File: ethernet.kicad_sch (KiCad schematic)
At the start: 44 parts, among them J6 Bus_RJ45_5-2337992-8, Q17 PJE138K, U22 TPS2372-3RGWR, U23 ULS-12_5-D48N-C, U39 ACPL-217-500E

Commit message: Init commit
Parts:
- C52, C78: LCSC Part # (none) -> C85960
- C76: LCSC Part # (none) -> C28233
- C77: LCSC Part # (none) -> C597086
- C79, C80, C81, C82: LCSC Part # (none) -> C529057
- C84, C85: LCSC Part # (none) -> C2167809
- D12, D13: LCSC Part # (none) -> C3151657
- D14: LCSC Part # (none) -> C272849
- D15: LCSC Part # (none) -> C125093
- FB2, FB3: LCSC Part # (none) -> C85840
- J6: LCSC Part # (none) -> C6393472
- Q17: LCSC Part # (none) -> C391643
- R129, R241: LCSC Part # (none) -> C242160
- R142: LCSC Part # (none) -> C2076619
- R145: LCSC Part # (none) -> C2089885
- R147, R151, R152: LCSC Part # (none) -> C19946422
- R148, R149, R150, R153: LCSC Part # (none) -> C202396
- R155, R156: LCSC Part # (none) -> C202394
- R157, R243: LCSC Part # (none) -> C512908
- R185, R229: LCSC Part # (none) -> C2077080
- R198, R199: LCSC Part # (none) -> C2085488
- U22: LCSC Part # (none) -> C2876734
- U23: LCSC Part # (none) -> C7136871
- U39: LCSC Part # (none) -> C2939626

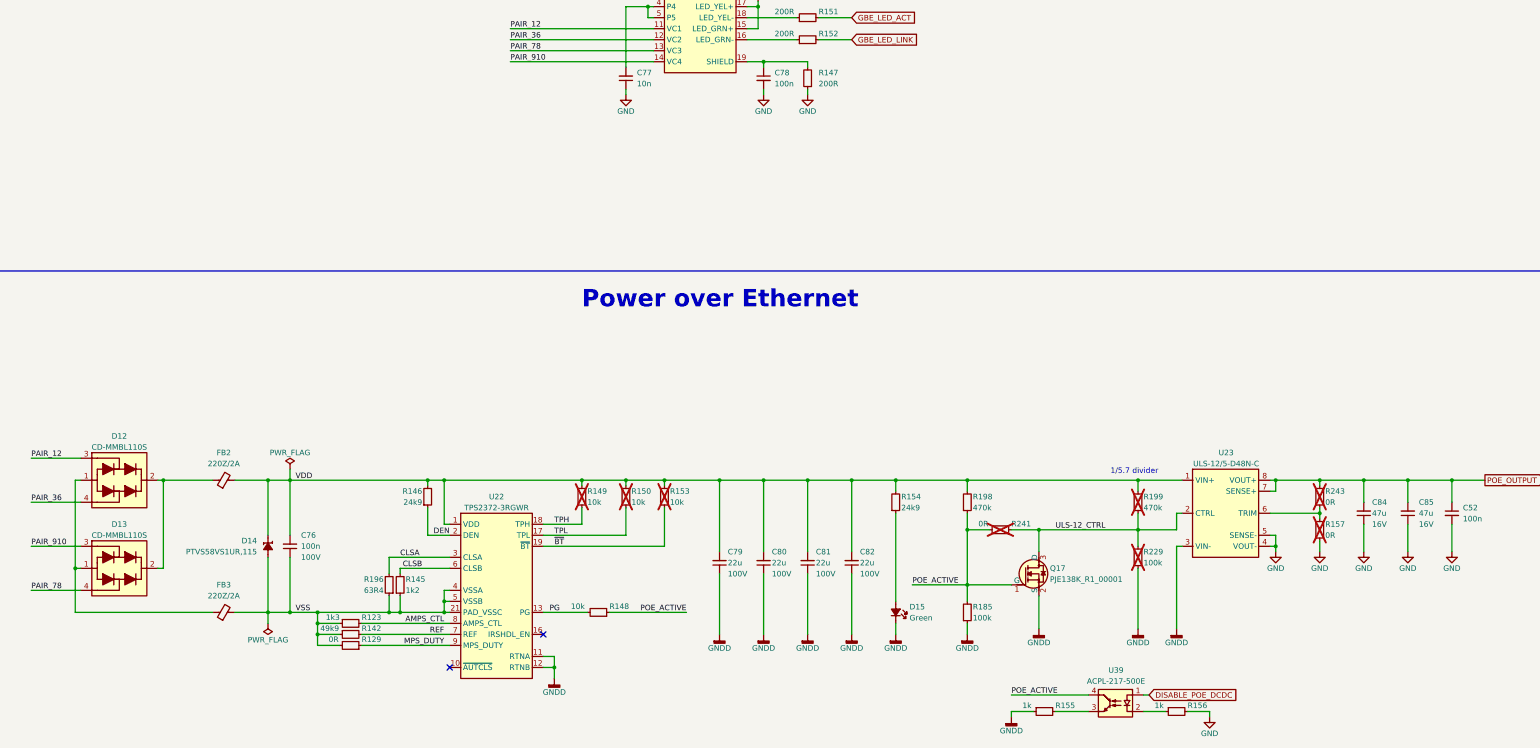
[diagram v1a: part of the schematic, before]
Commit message: Add field Digikey Part Number. Add Chinese substitute components
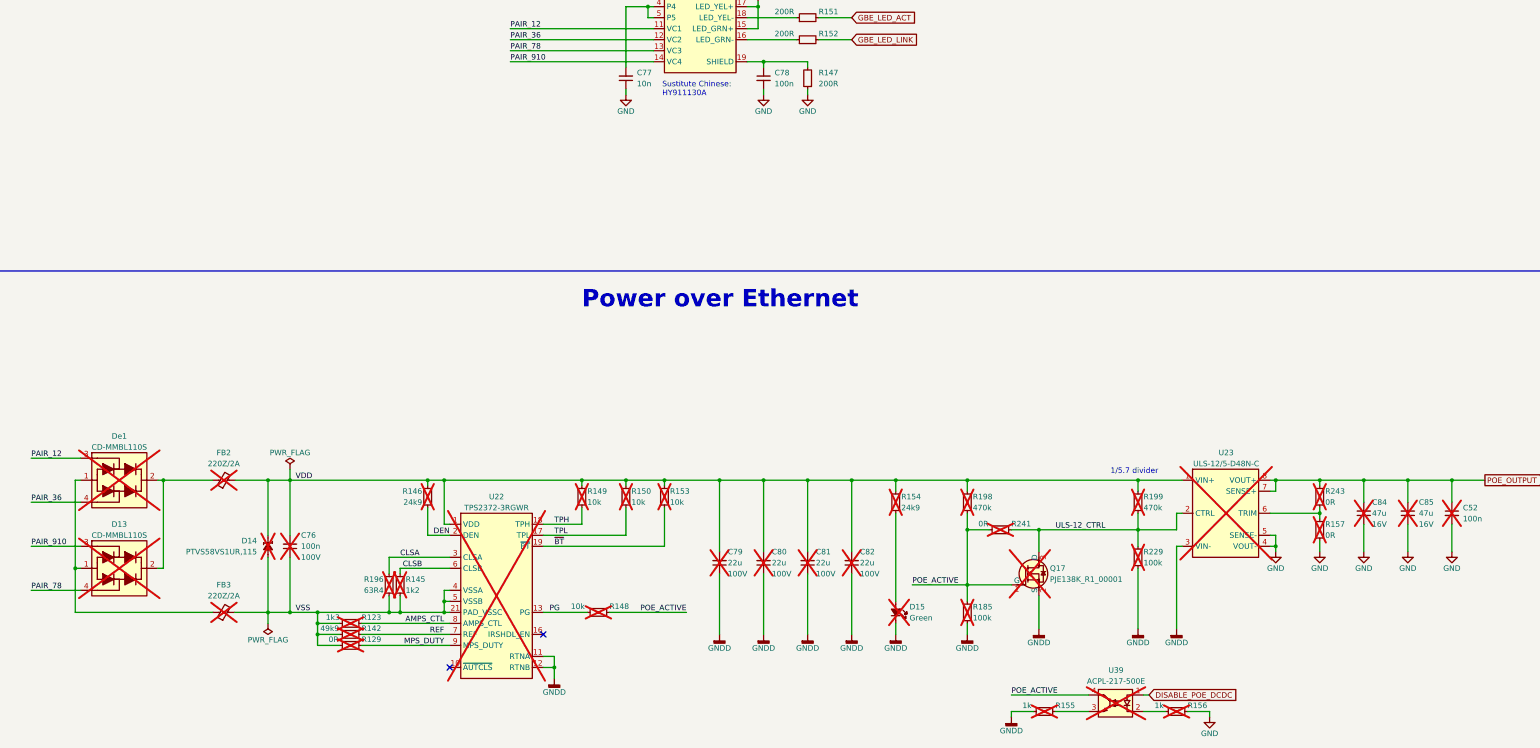
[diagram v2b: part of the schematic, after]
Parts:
- C52: Digikey Part # (none) -> 490-10697-1-ND; now not fitted; now left out of the parts list
- C76: now not fitted; now left out of the parts list
- C77: Digikey Part # (none) -> 478-KGM15AR72A103JTCT-ND
- C78: Digikey Part # (none) -> 490-10697-1-ND
- C79, C80, C81, C82: Digikey Part # (none) -> 445-C5750X7S2A226M280KBCT-ND; now not fitted; now left out of the parts list
- C84, C85: Digikey Part # (none) -> 445-6003-1-ND; now not fitted; now left out of the parts list
- D13: Digikey Part # (none) -> 118-CD-MMBL110SCT-ND; now not fitted; now left out of the parts list
- D14: Digikey Part # (none) -> 1727-PTVS58VS1UR,115CT-ND; now not fitted; now left out of the parts list
- D15: Digikey Part # (none) -> 160-1183-1-ND; now not fitted; now left out of the parts list
- De1: renamed from D12; Digikey Part # (none) -> 118-CD-MMBL110SCT-ND; now not fitted; now left out of the parts list
- FB2, FB3: Digikey Part # (none) -> 490-1054-1-ND; now not fitted; now left out of the parts list
- Q17: Digikey Part # (none) -> 3757-PJE138K_R1_00001CT-ND; now not fitted; now left out of the parts list
- R123: Digikey Part # (none) -> CR0402-FX-1301GLFCT-ND; now not fitted; now left out of the parts list
- R129: Digikey Part # (none) -> P0.0JCT-ND; now not fitted; now left out of the parts list
- R142: Digikey Part # (none) -> CR0402-FX-4992GLFCT-ND; now not fitted; now left out of the parts list
- R145: Digikey Part # (none) -> CR0402-FX-1201GLFCT-ND; now not fitted; now left out of the parts list
- R146, R154: Digikey Part # (none) -> CR0402-FX-2492GLFCT-ND; now not fitted; now left out of the parts list
- R147, R151, R152: Digikey Part # (none) -> CR0402-FX-2000GLFCT-ND
- R148: Digikey Part # (none) -> CR0402-FX-1002GLFCT-ND; now not fitted; now left out of the parts list
- R149, R150, R153: Digikey Part # (none) -> CR0402-FX-1002GLFCT-ND
- R155, R156: Digikey Part # (none) -> CR0402-FX-1001GLFCT-ND; now not fitted; now left out of the parts list
- R157, R243: Digikey Part # (none) -> CR0603-J/-000ELFCT-ND
- R185: Digikey Part # (none) -> CR0402-FX-1003GLFCT-ND; now not fitted; now left out of the parts list
- R196: Digikey Part # (none) -> 118-CR0603-FX-63R4ELFCT-ND; now not fitted; now left out of the parts list
- R198: Digikey Part # (none) -> CR0402-FX-4703GLFCT-ND; now not fitted; now left out of the parts list
- R199: Digikey Part # (none) -> CR0402-FX-4703GLFCT-ND
- R229: Digikey Part # (none) -> CR0402-FX-1003GLFCT-ND
- R241: Digikey Part # (none) -> P0.0JCT-ND
- U22: Digikey Part # (none) -> 296-51871-1-ND; now not fitted; now left out of the parts list
- U23: Digikey Part # (none) -> 811-2198-ND; now not fitted; now left out of the parts list
- U39: Digikey Part # (none) -> 516-1978-1-ND; now not fitted; now left out of the parts list
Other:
- note added: "Sustitute Chinese: HY911130A"
